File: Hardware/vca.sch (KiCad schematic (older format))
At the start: 19 parts, among them Q1 MMBFJ177, Q2 MMBFJ177, Q3 MMBFJ177, Q4 MMBFJ177, SW1 SW_DPDT_x2, SW2 SW_DPDT_x2, U4 TL074

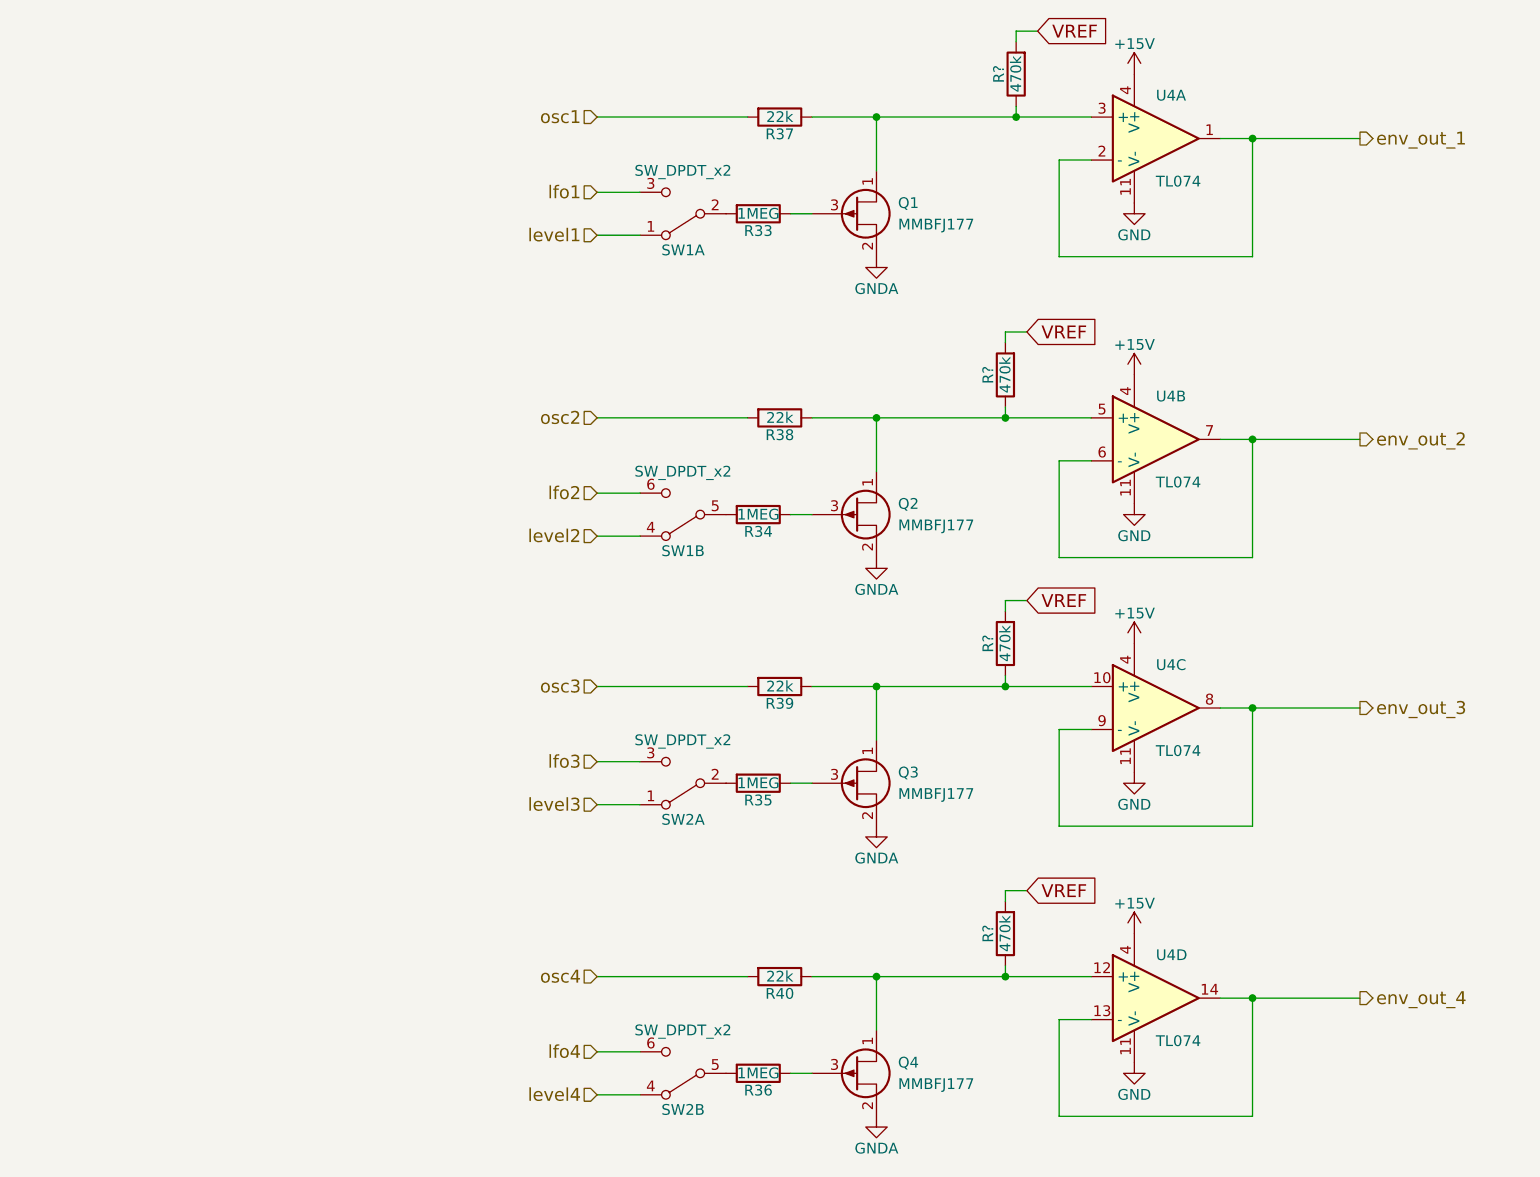
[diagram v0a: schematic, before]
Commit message: change corner frequency of DC blocking caps  everywhere they are in use.  Updated some simulation files to test filter circuits.
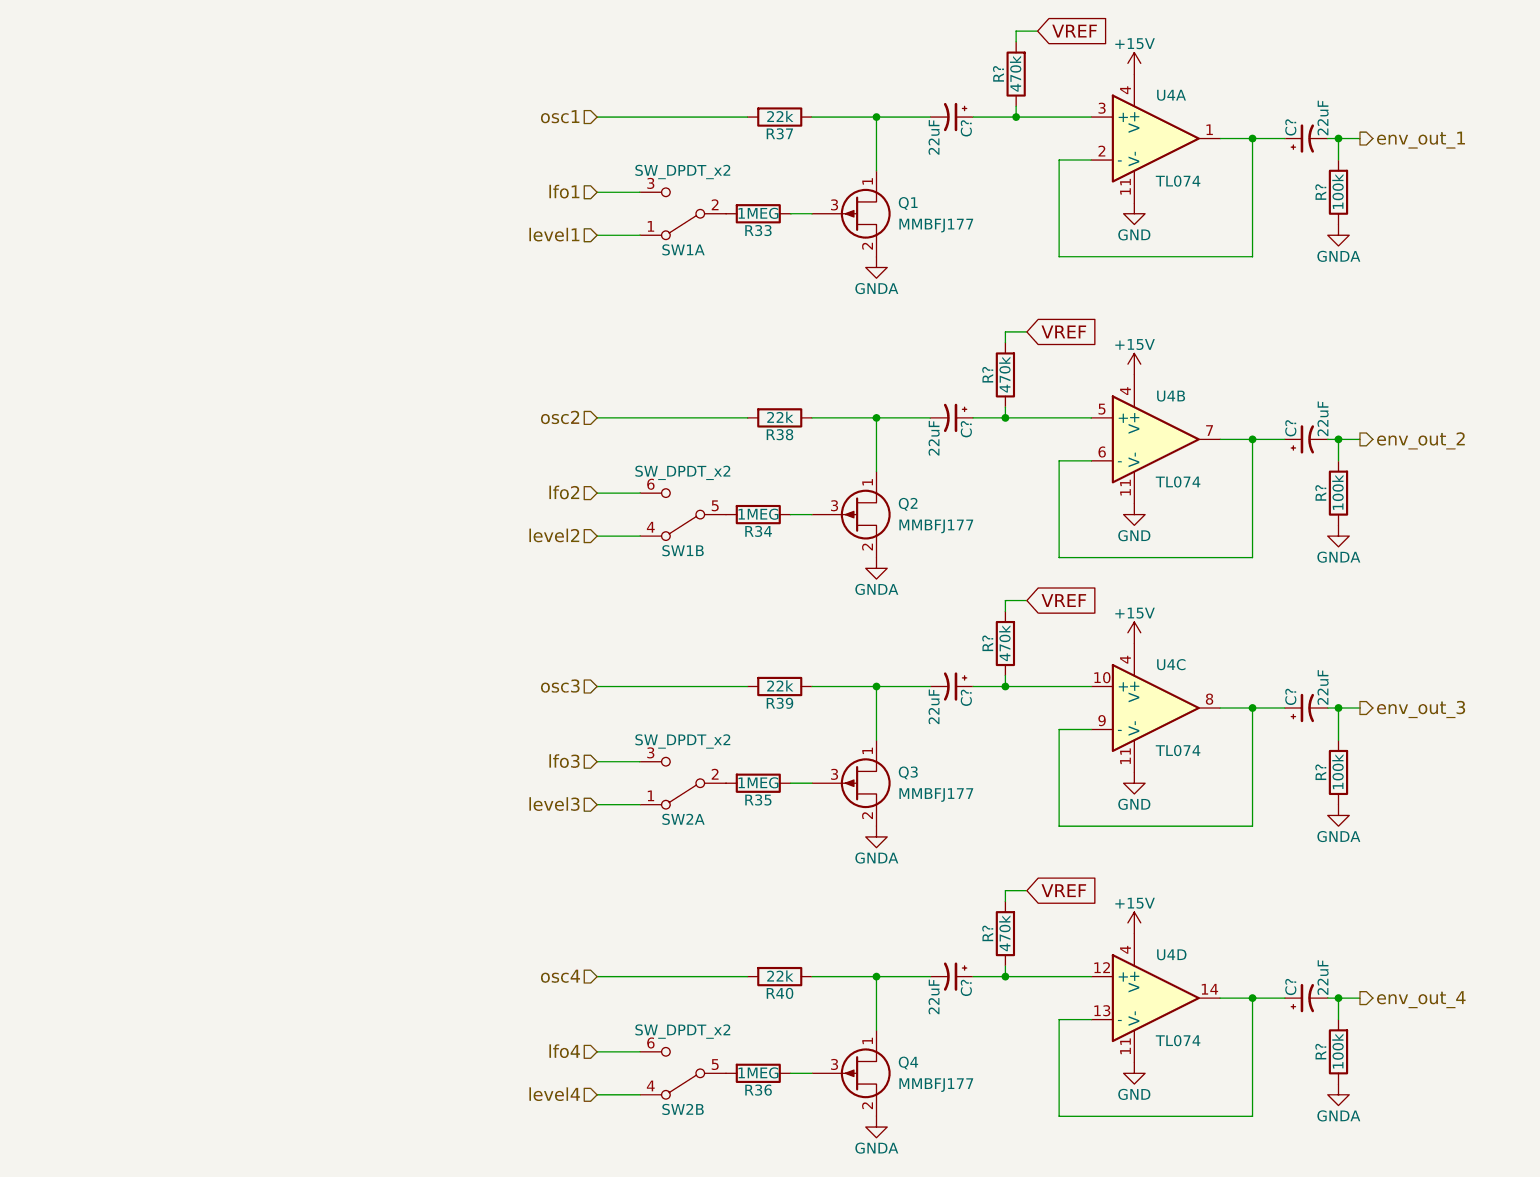
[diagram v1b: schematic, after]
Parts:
- added C? (x8): 22uF, symbol CP1_Small
- added R? (x4): 100k, symbol R
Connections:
- net GNDA: now also R?.1, R?.1, R?.1, R?.1
- net env_out_1: now also C?.2, R?.2; no longer U4.1, U4.2 (-)
- net env_out_2: now also C?.2, R?.2; no longer U4.6 (-), U4.7
- net env_out_3: now also C?.2, R?.2; no longer U4.8, U4.9 (-)
- net env_out_4: now also C?.2, R?.2; no longer U4.13 (-), U4.14
- net at Q1.1 (D), R37.1: now also C?.2; no longer R?.1, U4.3 (+)
- net at Q2.1 (D), R38.1: now also C?.2; no longer R?.1, U4.5 (+)
- net at Q3.1 (D), R39.1: now also C?.2; no longer R?.1, U4.10 (+)
- net at Q4.1 (D), R40.1: now also C?.2; no longer R?.1, U4.12 (+)
- new net: C?.1, U4.1, U4.2 (-)
- new net: C?.1, R?.1, U4.3 (+)
- new net: C?.1, R?.1, U4.5 (+)
- new net: C?.1, U4.6 (-), U4.7
- new net: C?.1, R?.1, U4.10 (+)
- new net: C?.1, U4.8, U4.9 (-)
- new net: C?.1, R?.1, U4.12 (+)
- new net: C?.1, U4.13 (-), U4.14
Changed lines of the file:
@@
 $EndComp
-Wire Wire Line
-	6150 1050 6800 1050
 Wire Wire Line
 	6300 1050 6300 1600
@@
 $EndComp
 Wire Wire Line
-	4250 950  5550 950
-Wire Wire Line
 	3950 950  3250 950
 Wire Wire Line
@@
 $EndComp
 Wire Wire Line
-	6150 2450 6800 2450
-Wire Wire Line
 	6300 2450 6300 3000
 Wire Wire Line
@@
 $EndComp
 Wire Wire Line
-	4250 2350 5550 2350
-Wire Wire Line
 	3950 2350 3250 2350
 Wire Wire Line
@@
 $EndComp
 Wire Wire Line
-	6150 3700 6800 3700
-Wire Wire Line
 	6300 3700 6300 4250
 Wire Wire Line
@@
 $EndComp
 Wire Wire Line
-	4250 3600 5550 3600
-Wire Wire Line
 	3950 3600 3250 3600
 Wire Wire Line
@@
 $EndComp
 Wire Wire Line
-	6150 5050 6800 5050
-Wire Wire Line
 	6300 5050 6300 5600
 Wire Wire Line
@@
 $EndComp
 Wire Wire Line
-	4250 4950 5550 4950
-Wire Wire Line
 	3950 4950 3250 4950
 Wire Wire Line
@@
 	5150 2300 5150 2350
 Connection ~ 5150 2350
+$Comp
+L CP1_Small C?
+U 1 1 5C37B22A
+P 4900 950
+F 0 "C?" H 4910 1020 50  0000 L CNN
+F 1 "22uF" H 4910 870 50  0000 L CNN
+F 2 "" H 4900 950 50  0001 C CNN
+F 3 "" H 4900 950 50  0001 C CNN
+	1    4900 950
+	0    1    1    0
+$EndComp
+$Comp
+L CP1_Small C?
+U 1 1 5C37B322
+P 4900 2350
+F 0 "C?" H 4910 2420 50  0000 L CNN
+F 1 "22uF" H 4910 2270 50  0000 L CNN
+F 2 "" H 4900 2350 50  0001 C CNN
+F 3 "" H 4900 2350 50  0001 C CNN
+	1    4900 2350
+	0    1    1    0
+$EndComp
+$Comp
+L CP1_Small C?
+U 1 1 5C37B4FA
+P 4900 3600
+F 0 "C?" H 4910 3670 50  0000 L CNN
+F 1 "22uF" H 4910 3520 50  0000 L CNN
+F 2 "" H 4900 3600 50  0001 C CNN
+F 3 "" H 4900 3600 50  0001 C CNN
+	1    4900 3600
+	0    1    1    0
+$EndComp
+$Comp
+L CP1_Small C?
+U 1 1 5C37B589
+P 4900 4950
+F 0 "C?" H 4910 5020 50  0000 L CNN
+F 1 "22uF" H 4910 4870 50  0000 L CNN
+F 2 "" H 4900 4950 50  0001 C CNN
+F 3 "" H 4900 4950 50  0001 C CNN
+	1    4900 4950
+	0    1    1    0
+$EndComp
+$Comp
+L CP1_Small C?
+U 1 1 5C37B623
+P 6550 1050
+F 0 "C?" H 6560 1120 50  0000 L CNN
+F 1 "22uF" H 6560 970 50  0000 L CNN
+F 2 "" H 6550 1050 50  0001 C CNN
+F 3 "" H 6550 1050 50  0001 C CNN
+	1    6550 1050
+	0    -1   -1   0
+$EndComp
+$Comp
+L CP1_Small C?
+U 1 1 5C37B6D4
+P 6550 2450
+F 0 "C?" H 6560 2520 50  0000 L CNN
+F 1 "22uF" H 6560 2370 50  0000 L CNN
+F 2 "" H 6550 2450 50  0001 C CNN
+F 3 "" H 6550 2450 50  0001 C CNN
+	1    6550 2450
+	0    -1   -1   0
+$EndComp
+$Comp
+L CP1_Small C?
+U 1 1 5C37B778
+P 6550 3700
+F 0 "C?" H 6560 3770 50  0000 L CNN
+F 1 "22uF" H 6560 3620 50  0000 L CNN
+F 2 "" H 6550 3700 50  0001 C CNN
+F 3 "" H 6550 3700 50  0001 C CNN
+	1    6550 3700
+	0    -1   -1   0
+$EndComp
+$Comp
+L CP1_Small C?
+U 1 1 5C37B81B
+P 6550 5050
+F 0 "C?" H 6560 5120 50  0000 L CNN
+F 1 "22uF" H 6560 4970 50  0000 L CNN
+F 2 "" H 6550 5050 50  0001 C CNN
+F 3 "" H 6550 5050 50  0001 C CNN
+	1    6550 5050
+	0    -1   -1   0
+$EndComp
+$Comp
+L R R?
+U 1 1 5C37B8E3
+P 6700 1300
+F 0 "R?" V 6780 1300 50  0000 C CNN
+F 1 "100k" V 6700 1300 50  0000 C CNN
+F 2 "" V 6630 1300 50  0001 C CNN
+F 3 "" H 6700 1300 50  0001 C CNN
+	1    6700 1300
+	-1   0    0    1
+$EndComp
+$Comp
+L R R?
+U 1 1 5C37B9C7
+P 6700 2700
+F 0 "R?" V 6780 2700 50  0000 C CNN
+F 1 "100k" V 6700 2700 50  0000 C CNN
+F 2 "" V 6630 2700 50  0001 C CNN
+F 3 "" H 6700 2700 50  0001 C CNN
+	1    6700 2700
+	-1   0    0    1
+$EndComp
+$Comp
+L R R?
+U 1 1 5C37BADF
+P 6700 4000
+F 0 "R?" V 6780 4000 50  0000 C CNN
+F 1 "100k" V 6700 4000 50  0000 C CNN
+F 2 "" V 6630 4000 50  0001 C CNN
+F 3 "" H 6700 4000 50  0001 C CNN
+	1    6700 4000
+	-1   0    0    1
+$EndComp
+$Comp
+L R R?
+U 1 1 5C37BBB7
+P 6700 5300
+F 0 "R?" V 6780 5300 50  0000 C CNN
+F 1 "100k" V 6700 5300 50  0000 C CNN
+F 2 "" V 6630 5300 50  0001 C CNN
+F 3 "" H 6700 5300 50  0001 C CNN
+	1    6700 5300
+	-1   0    0    1
+$EndComp
+$Comp
+L GNDA #PWR?
+U 1 1 5C37BC69
+P 6700 1450
+F 0 "#PWR?" H 6700 1200 50  0001 C CNN
+F 1 "GNDA" H 6700 1300 50  0000 C CNN
+F 2 "" H 6700 1450 50  0001 C CNN
+F 3 "" H 6700 1450 50  0001 C CNN
+	1    6700 1450
+	1    0    0    -1
+$EndComp
+$Comp
+L GNDA #PWR?
+U 1 1 5C37BCE0
+P 6700 2850
+F 0 "#PWR?" H 6700 2600 50  0001 C CNN
+F 1 "GNDA" H 6700 2700 50  0000 C CNN
+F 2 "" H 6700 2850 50  0001 C CNN
+F 3 "" H 6700 2850 50  0001 C CNN
+	1    6700 2850
+	1    0    0    -1
+$EndComp
+$Comp
+L GNDA #PWR?
+U 1 1 5C37BD57
+P 6700 4150
+F 0 "#PWR?" H 6700 3900 50  0001 C CNN
+F 1 "GNDA" H 6700 4000 50  0000 C CNN
+F 2 "" H 6700 4150 50  0001 C CNN
+F 3 "" H 6700 4150 50  0001 C CNN
+	1    6700 4150
+	1    0    0    -1
+$EndComp
+$Comp
+L GNDA #PWR?
+U 1 1 5C37BDCE
+P 6700 5450
+F 0 "#PWR?" H 6700 5200 50  0001 C CNN
+F 1 "GNDA" H 6700 5300 50  0000 C CNN
+F 2 "" H 6700 5450 50  0001 C CNN
+F 3 "" H 6700 5450 50  0001 C CNN
+	1    6700 5450
+	1    0    0    -1
+$EndComp
+Wire Wire Line
+	4250 950  4800 950
+Wire Wire Line
+	5000 950  5550 950
+Wire Wire Line
+	5000 2350 5550 2350
+Wire Wire Line
+	4250 2350 4800 2350
+Wire Wire Line
+	4250 3600 4800 3600
+Wire Wire Line
+	5000 3600 5550 3600
+Wire Wire Line
+	4250 4950 4800 4950
+Wire Wire Line
+	5000 4950 5550 4950
+Wire Wire Line
+	6150 1050 6450 1050
+Wire Wire Line
+	6650 1050 6800 1050
+Wire Wire Line
+	6700 1150 6700 1050
+Connection ~ 6700 1050
+Wire Wire Line
+	6150 2450 6450 2450
+Wire Wire Line
+	6650 2450 6800 2450
+Wire Wire Line
+	6700 2550 6700 2450
+Connection ~ 6700 2450
+Wire Wire Line
+	6150 3700 6450 3700
+Wire Wire Line
+	6650 3700 6800 3700
+Wire Wire Line
+	6700 3850 6700 3700
+Connection ~ 6700 3700
+Wire Wire Line
+	6150 5050 6450 5050
+Wire Wire Line
+	6650 5050 6800 5050
+Wire Wire Line
+	6700 5150 6700 5050
+Connection ~ 6700 5050
 $EndSCHEMATC

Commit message: add bias voltage to LFO control voltage at JFET gate. This is needed because the LFO tri wave has +/- amplitude.
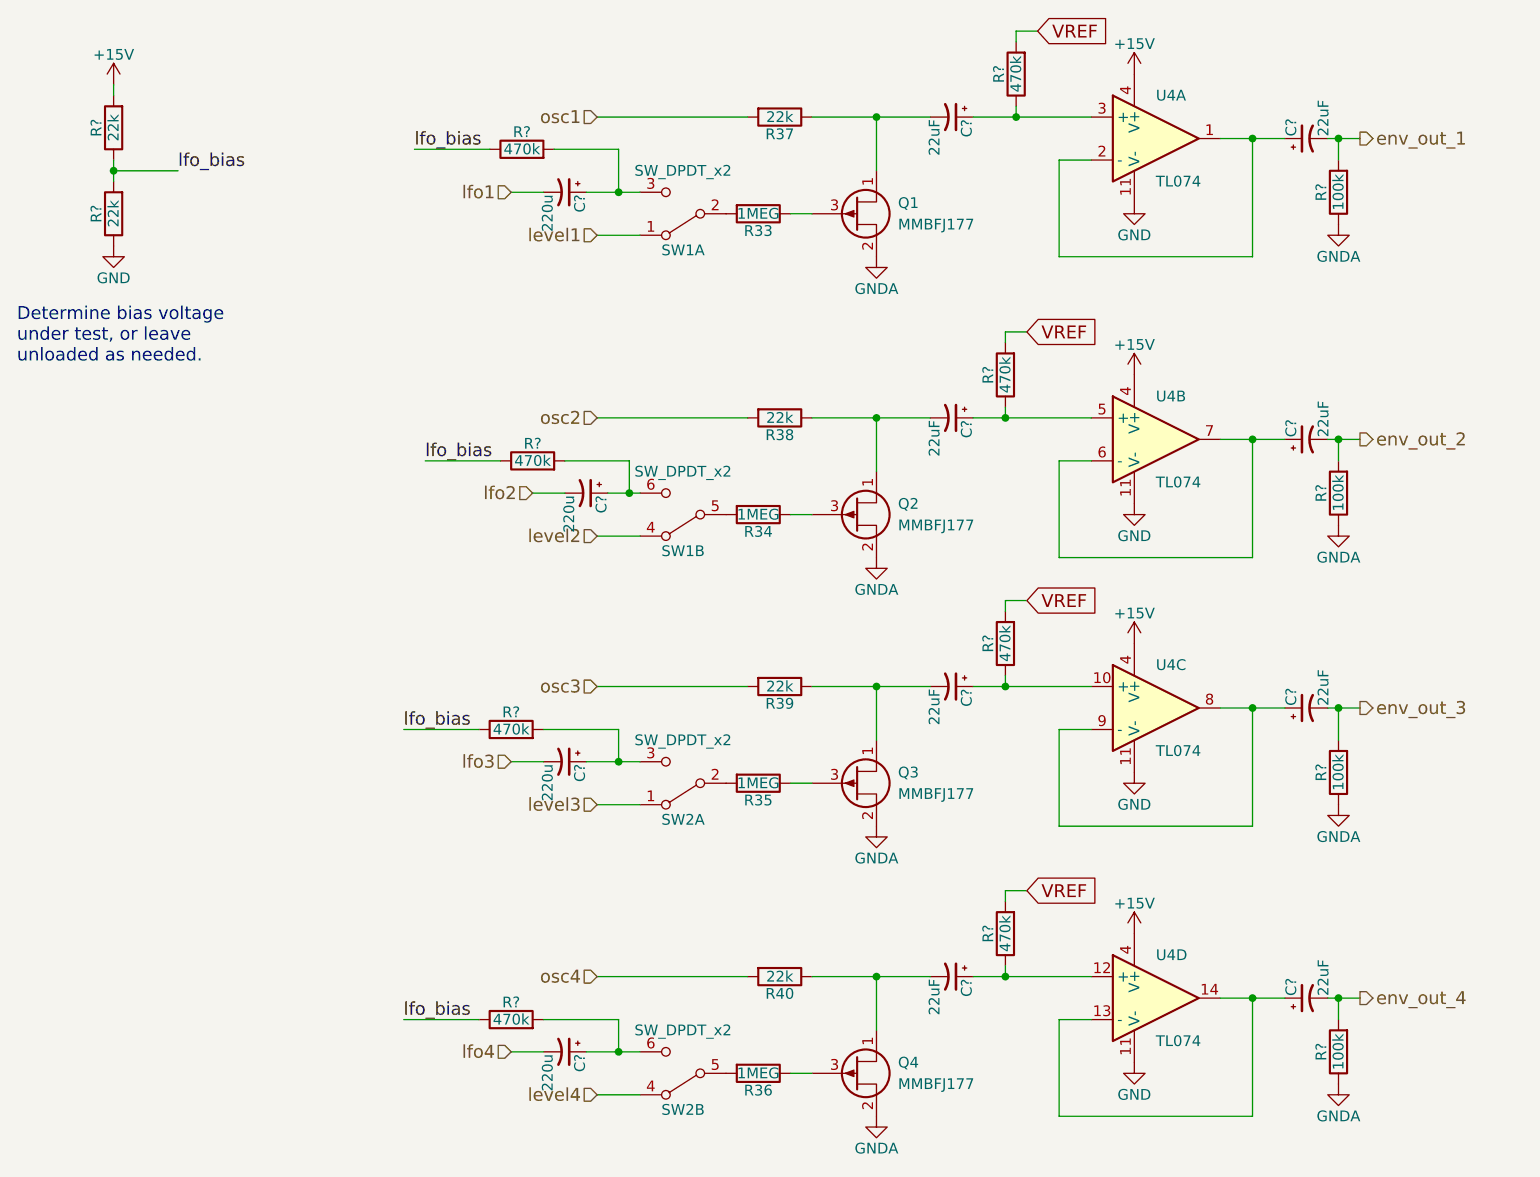
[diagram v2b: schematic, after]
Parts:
- added C? (x4): 220u, symbol CP1_Small
- added R? (x2): 22k, symbol R
- added R? (x4): 470k, symbol R
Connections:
- net +15V: now also R?.2
- net GND: now also R?.1
- net lfo1: now also C?.2; no longer SW1.3 (C)
- net lfo2: now also C?.2; no longer SW1.6 (C)
- net lfo3: now also C?.2; no longer SW2.3 (C)
- net lfo4: now also C?.2; no longer SW2.6 (C)
- new net: C?.1, R?.2, SW1.3 (C)
- new net: C?.1, R?.2, SW1.6 (C)
- new net: C?.1, R?.2, SW2.3 (C)
- new net: C?.1, R?.2, SW2.6 (C)
- new net lfo_bias: R?.1, R?.1, R?.1, R?.1, R?.1, R?.2
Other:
- note added: "Determine bias voltage \nunder test, or leave \nunloaded as needed."

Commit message: begin to add taper to potentiometers. I think they're all right, but some tapers may change under test.
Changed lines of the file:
@@
 Text HLabel 2850 1300 0    60   Input ~ 0
 lfo1
-Text HLabel 3250 1500 0    60   Input ~ 0
+Text HLabel 2900 1500 0    60   Input ~ 0
 level1
 $Comp
@@
 Text HLabel 2950 2700 0    60   Input ~ 0
 lfo2
-Text HLabel 3250 2900 0    60   Input ~ 0
+Text HLabel 2950 2900 0    60   Input ~ 0
 level2
 $Comp
@@
 Text HLabel 2850 3950 0    60   Input ~ 0
 lfo3
-Text HLabel 3250 4150 0    60   Input ~ 0
+Text HLabel 2850 4150 0    60   Input ~ 0
 level3
 $Comp
@@
 Text HLabel 2850 5300 0    60   Input ~ 0
 lfo4
-Text HLabel 3250 5500 0    60   Input ~ 0
+Text HLabel 2850 5500 0    60   Input ~ 0
 level4
 $Comp
@@
 	3350 1300 3450 1300
 Wire Wire Line
-	3250 1500 3450 1500
+	2900 1500 3450 1500
 Connection ~ 6300 1050
 Wire Wire Line
@@
 	3400 2700 3450 2700
 Wire Wire Line
-	3250 2900 3450 2900
+	2950 2900 3450 2900
 Connection ~ 6300 2450
 Wire Wire Line
@@
 	3350 3950 3450 3950
 Wire Wire Line
-	3250 4150 3450 4150
+	2850 4150 3450 4150
 Connection ~ 6300 3700
 Wire Wire Line
@@
 	3350 5300 3450 5300
 Wire Wire Line
-	3250 5500 3450 5500
+	2850 5500 3450 5500
 Connection ~ 6300 5050
 Wire Wire Line
